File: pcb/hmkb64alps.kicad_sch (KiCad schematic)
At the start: 15 parts, among them SW1 SW_Push, U1 ATmega32U4-A, Y1 16MHz

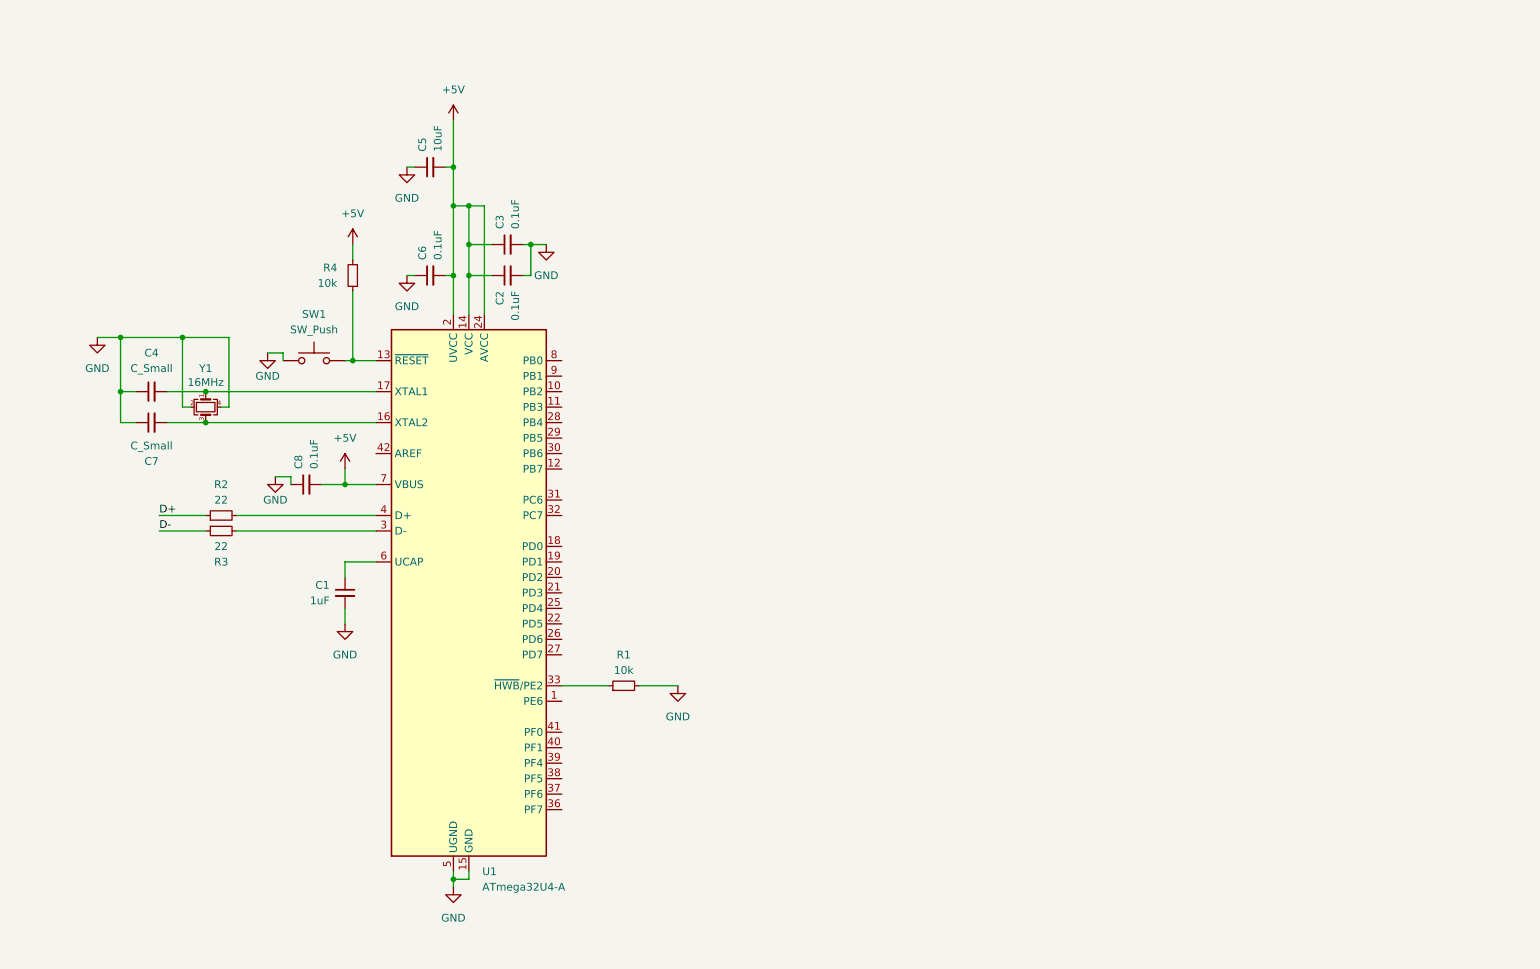
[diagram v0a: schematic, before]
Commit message: add usb-c and ISP to mcu schematic
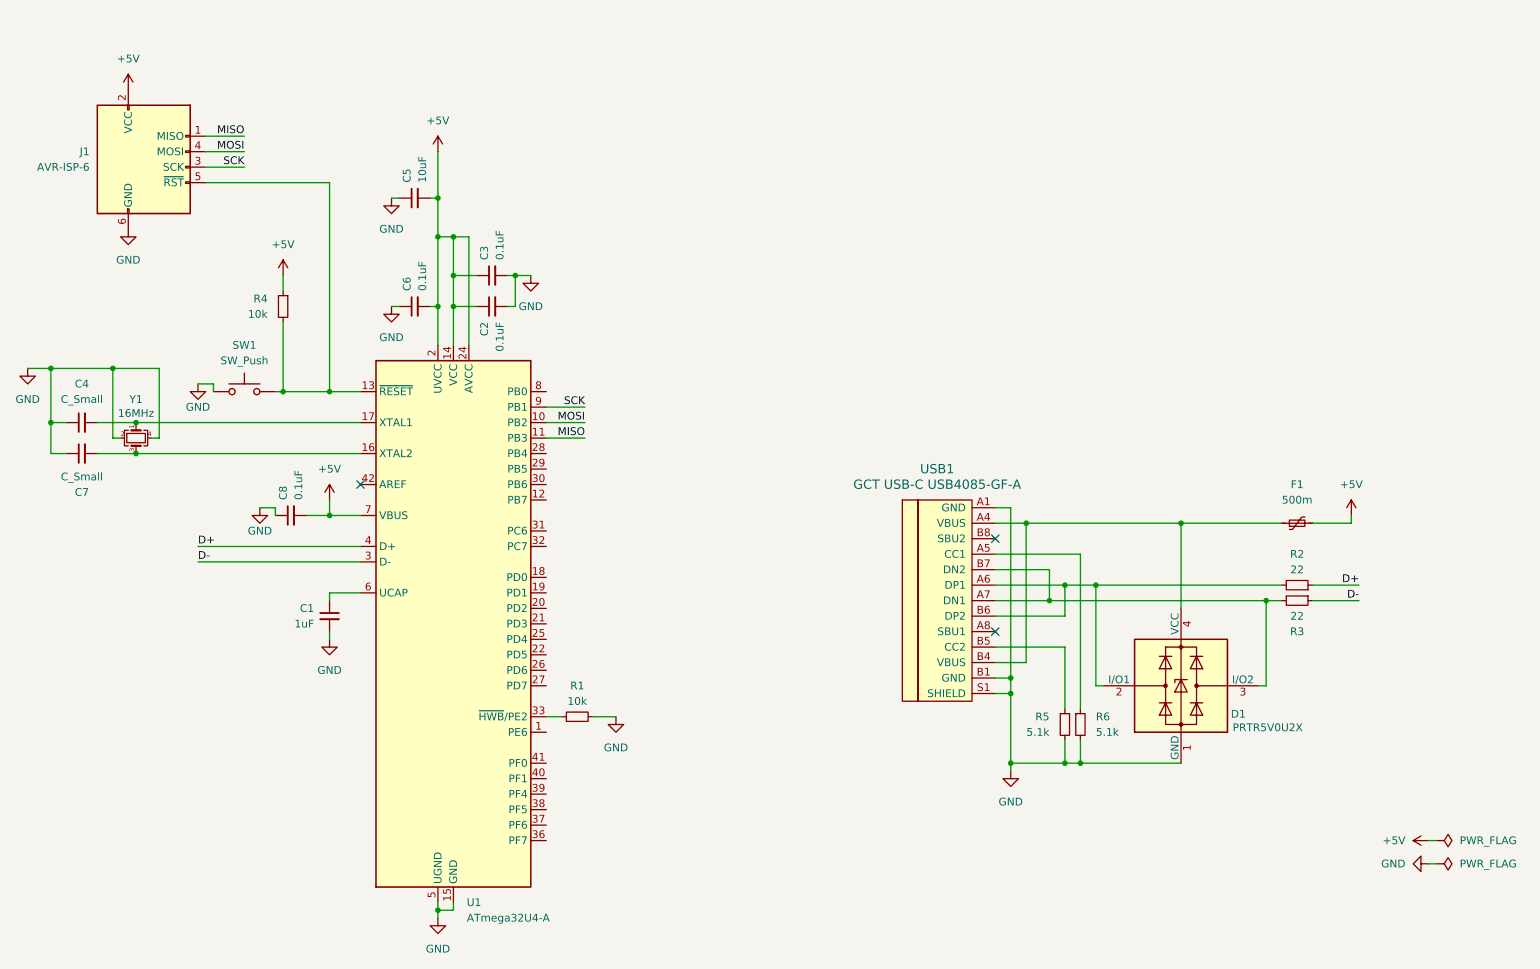
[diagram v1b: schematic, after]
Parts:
- added D1: PRTR5V0U2X, Package_TO_SOT_SMD:SOT-143, symbol Power_Protection:PRTR5V0U2X
- added F1: 500m, symbol Device:Polyfuse_Small
- added J1: AVR-ISP-6, symbol Connector:AVR-ISP-6
- added R5, R6: 5.1k, symbol Device:R_Small
- added USB1: GCT USB-C USB4085-GF-A, symbol hmkb64alps:GCT USB-C USB4085-GF-A
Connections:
- net +5V: now also F1.2, J1.2 (VCC)
- net D+: now also U1.4 (D+)
- net D-: now also U1.3 (D-)
- net GND: now also D1.1 (GND), J1.6 (GND), R5.2, R6.2, USB1.A1 (GND), USB1.A12 (GND), USB1.B1 (GND), USB1.B12 (GND), USB1.S1 (SHIELD)
- net at R3.2: now also D1.3 (I/O2), USB1.A7 (DN1), USB1.B7 (DN2); no longer U1.3 (D-)
- net MOSI: now reaches U1.10 (PB2)
- net MOSI: now also J1.4 (MOSI)
- net MISO: now reaches U1.11 (PB3)
- net MISO: now also J1.1 (MISO)
- net at R4.2, SW1.2, U1.13 (~{RESET}): now also J1.5 (~{RST})
- net at R2.2: now also D1.2 (I/O1), USB1.A6 (DP1), USB1.B6 (DP2); no longer U1.4 (D+)
- net SCK: now reaches U1.9 (PB1)
- net SCK: now also J1.3 (SCK)
- new net: R5.1, USB1.B5 (CC2)
- new net: D1.4 (VCC), F1.1, USB1.A4 (VBUS), USB1.A9 (VBUS), USB1.B4 (VBUS), USB1.B9 (VBUS)
- new net: R6.1, USB1.A5 (CC1)
- no-connect marks 0 -> 3
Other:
- moved on the sheet: C1, C2, C3, C4, C5, C6, C7, C8, R1, R2, R3, R4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

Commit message: add key key matrix to schematic
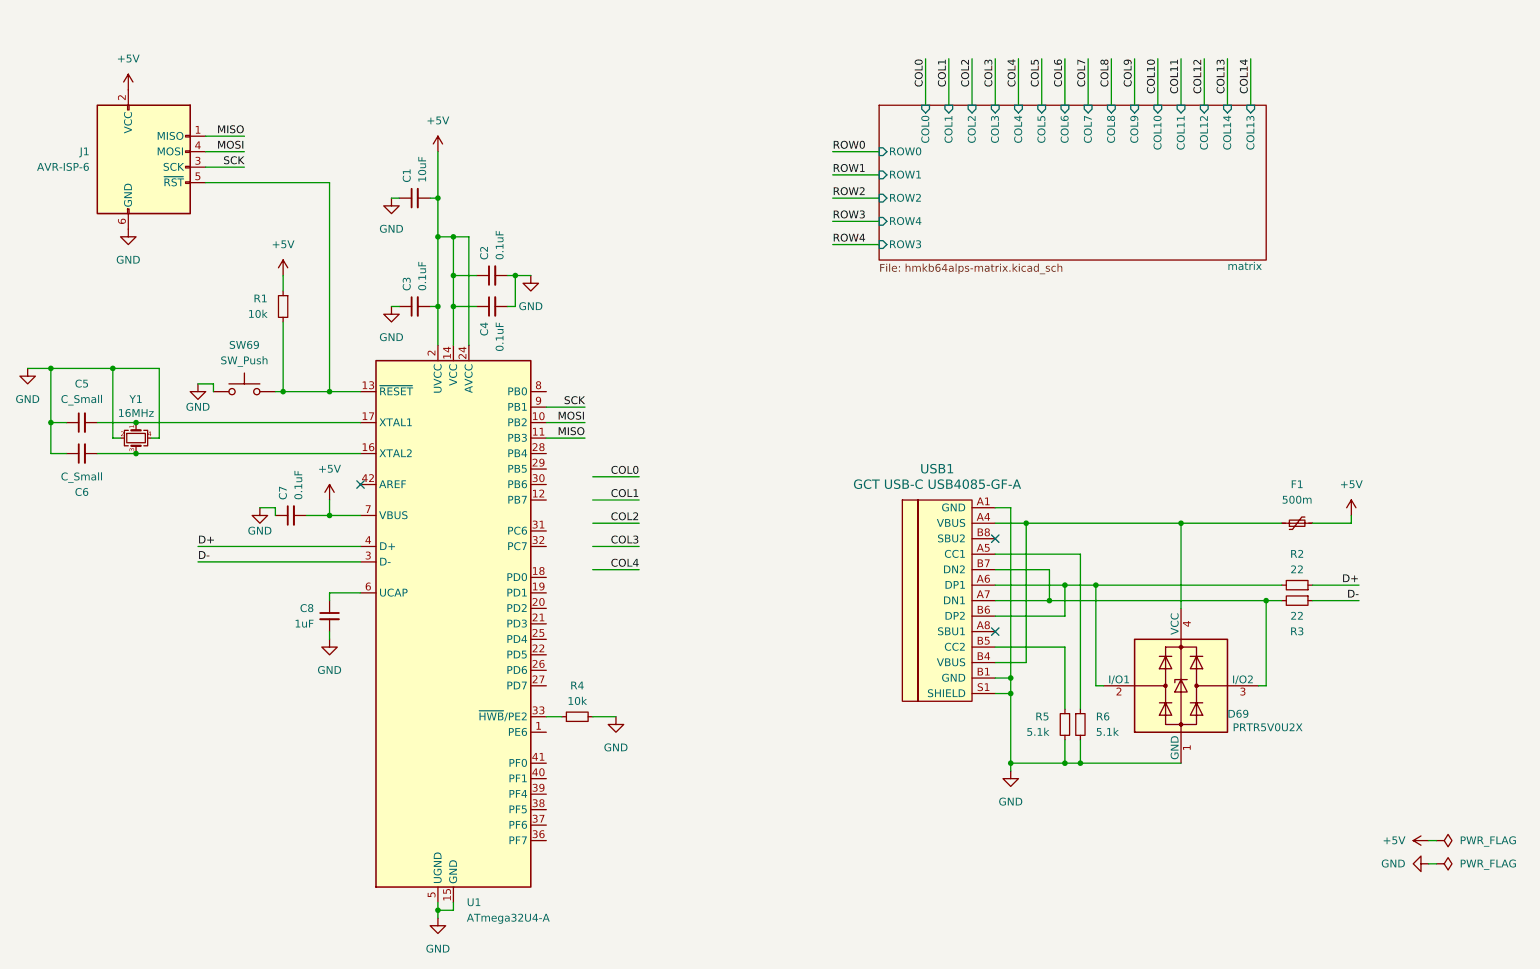
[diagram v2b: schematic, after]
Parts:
- C1: renamed from C5; footprint (none) -> Capacitor_SMD:C_0805_2012Metric_Pad1.18x1.45mm_HandSolder
- C2: renamed from C3; footprint (none) -> Capacitor_SMD:C_0805_2012Metric_Pad1.18x1.45mm_HandSolder
- C3: renamed from C6; footprint (none) -> Capacitor_SMD:C_0805_2012Metric_Pad1.18x1.45mm_HandSolder
- C4: renamed from C2; footprint (none) -> Capacitor_SMD:C_0805_2012Metric_Pad1.18x1.45mm_HandSolder
- C5: renamed from C4; footprint (none) -> Capacitor_SMD:C_0805_2012Metric_Pad1.18x1.45mm_HandSolder
- C6: renamed from C7; footprint (none) -> Capacitor_SMD:C_0805_2012Metric_Pad1.18x1.45mm_HandSolder
- C7: renamed from C8; footprint (none) -> Capacitor_SMD:C_0805_2012Metric_Pad1.18x1.45mm_HandSolder
- C8: renamed from C1; footprint (none) -> Capacitor_SMD:C_0805_2012Metric_Pad1.18x1.45mm_HandSolder
- F1: footprint (none) -> Fuse:Fuse_1206_3216Metric_Pad1.42x1.75mm_HandSolder
- J1: footprint (none) -> Connector_IDC:IDC-Header_2x03_P2.54mm_Vertical
- R1: renamed from R4; footprint (none) -> Resistor_SMD:R_0805_2012Metric_Pad1.20x1.40mm_HandSolder
- R2, R3, R5, R6: footprint (none) -> Resistor_SMD:R_0805_2012Metric_Pad1.20x1.40mm_HandSolder
- R4: renamed from R1; footprint (none) -> Resistor_SMD:R_0805_2012Metric_Pad1.20x1.40mm_HandSolder
- SW69: renamed from SW1; footprint (none) -> Button_Switch_SMD:SW_SPST_SKQG_WithStem
- USB1: footprint (none) -> ai03-2725_Type-C:USB_C_GCT_USB4085
- Y1: footprint (none) -> Crystal:Crystal_SMD_3225-4Pin_3.2x2.5mm_HandSoldering
- renumbered D1 to D69
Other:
- added sheet matrix (hmkb64alps-matrix.kicad_sch)

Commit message: revert to global labels for matrix
kbplacer does unfortunately not seem to work with local or hierarchical
labels (which I would have prefered). So global labels it is.
Essentially that means using the schematic generated by
`layout2schematic.py` works fine and best.
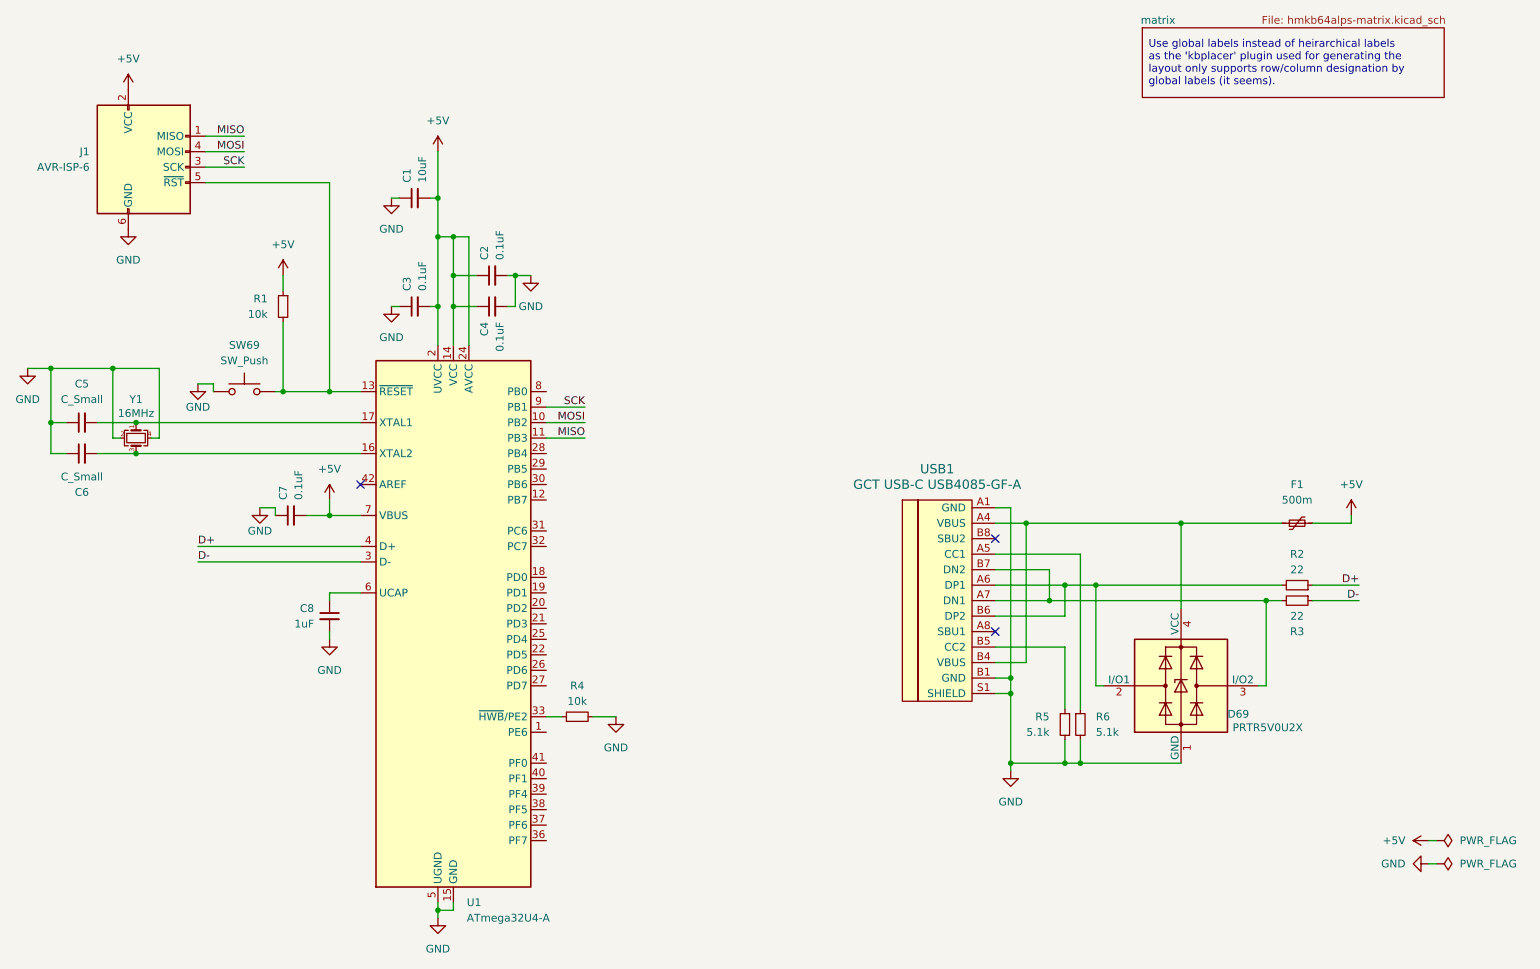
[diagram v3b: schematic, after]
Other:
- sheet matrix ports: added none; removed COL0, COL1, COL10, COL11, COL12, COL13, COL14, COL2, COL3, COL4, COL5, COL6, COL7, COL8, COL9, ROW0, ROW1, ROW2, ROW3, ROW4
- note added: "Use global labels instead of heirarchical labels as the 'kbplacer' plugin used for generating the layout only supports row/column designation by global labels (it seems)."

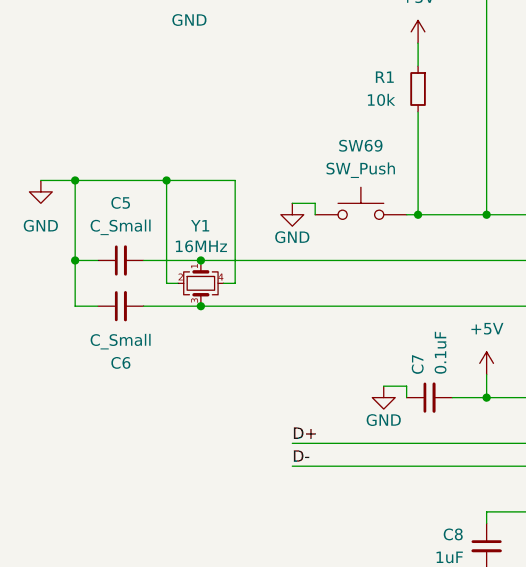
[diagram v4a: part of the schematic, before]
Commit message: add missing values for oscillator capacitors
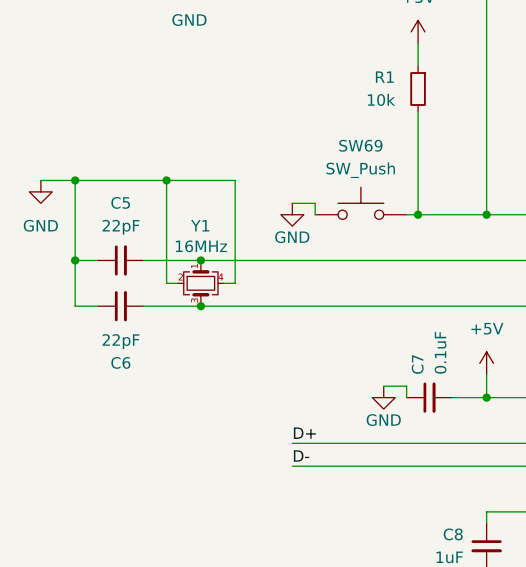
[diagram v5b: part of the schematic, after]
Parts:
- C5, C6: value C_Small -> 22pF
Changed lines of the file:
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@@
 			)
 		)
-		(property "Value" "C_Small"
+		(property "Value" "22pF"
 			(at 45.7263 85.09 90)
 			(effects
@@
 			)
 		)
-		(property "Value" "C_Small"
+		(property "Value" "22pF"
 			(at 45.7263 97.79 90)
 			(effects

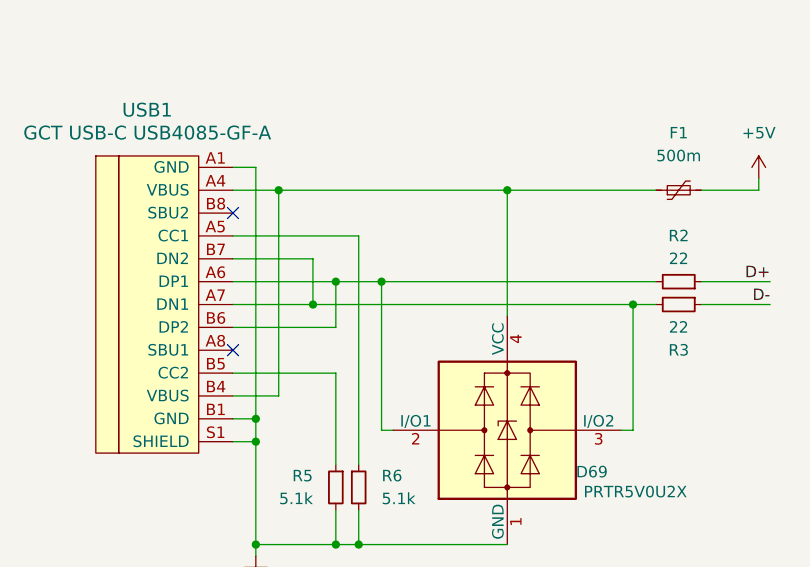
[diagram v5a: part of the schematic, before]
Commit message: roughly position mcu and sourrounding components
Also change to different usbc footprint
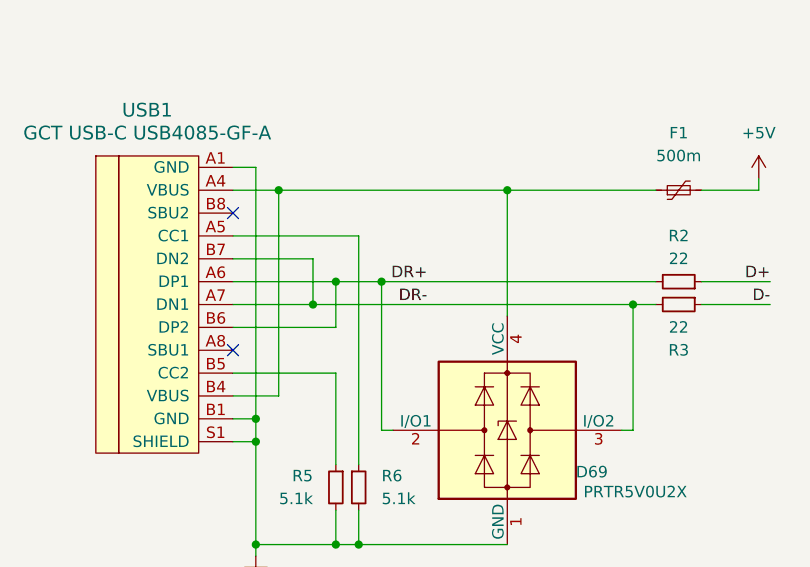
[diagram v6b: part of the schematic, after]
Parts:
- USB1: footprint ai03-2725_Type-C:USB_C_GCT_USB4085 -> Connector_USB:USB_C_Receptacle_HRO_TYPE-C-31-M-12
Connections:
- net DR-: now reaches D69.3 (I/O2), R3.2, USB1.A7 (DN1), USB1.B7 (DN2)
- net DR+: now reaches D69.2 (I/O1), R2.2, USB1.A6 (DP1), USB1.B6 (DP2)
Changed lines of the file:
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@@
 		)
 	)
-	(label "D-"
-		(at 64.77 111.76 0)
+	(label "DR+"
+		(at 217.17 115.57 180)
 		(fields_autoplaced yes)
 		(effects
@@
 				(size 1.27 1.27)
 			)
-			(justify left bottom)
-		)
-	)
-	(label "D+"
-		(at 64.77 109.22 0)
+			(justify right bottom)
+		)
+	)
+	(label "D-"
+		(at 64.77 111.76 0)
 		(fields_autoplaced yes)
 		(effects
@@
 	)
 	(label "D+"
-		(at 255.27 115.57 180)
+		(at 64.77 109.22 0)
 		(fields_autoplaced yes)
 		(effects
@@
 				(size 1.27 1.27)
 			)
-			(justify right bottom)
-		)
-	)
-	(label "MOSI"
-		(at 72.39 44.45 180)
+			(justify left bottom)
+		)
+	)
+	(label "D+"
+		(at 255.27 115.57 180)
 		(fields_autoplaced yes)
 		(effects
@@
 		)
 	)
+	(label "MOSI"
+		(at 72.39 44.45 180)
+		(fields_autoplaced yes)
+		(effects
+			(font
+				(size 1.27 1.27)
+			)
+			(justify right bottom)
+		)
+	)
 	(label "D-"
 		(at 255.27 118.11 180)
+		(fields_autoplaced yes)
+		(effects
+			(font
+				(size 1.27 1.27)
+			)
+			(justify right bottom)
+		)
+	)
+	(label "DR-"
+		(at 217.17 118.11 180)
 		(fields_autoplaced yes)
 		(effects
@@
 			)
 		)
-		(property "Footprint" "ai03-2725_Type-C:USB_C_GCT_USB4085"
+		(property "Footprint" "Connector_USB:USB_C_Receptacle_HRO_TYPE-C-31-M-12"
 			(at 191.77 116.84 0)
 			(effects
